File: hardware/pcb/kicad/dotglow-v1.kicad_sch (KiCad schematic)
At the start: 40 parts, among them J1 USB-C 5V, J2 DISPLAY IN, J3 DHT22, J4 I2C (RTC V2), J5 SPEAKER 8R 2W, J6 LDR, SW1 RESET, SW2 BOOT, SW3 STOPWATCH, U1 ESP32-S3-MINI-1-N8, U2 AP2112K-3.3, U3 74AHCT125, U4 MAX98357A, U5 USBLC6-2SC6

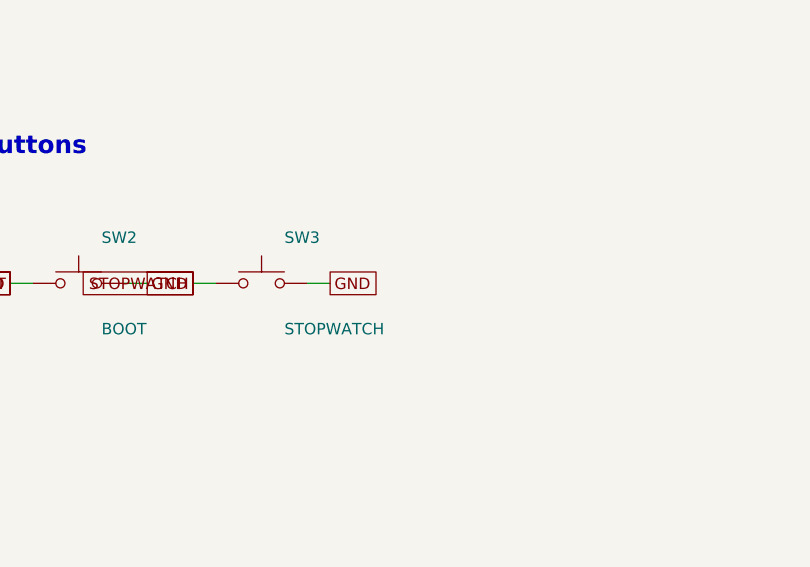
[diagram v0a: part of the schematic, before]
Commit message: DotGlow V1 board: stopwatch header J7, routing rerun, layout-only package for EasyEDA (outline, DXF, placement CSV)
Co-Authored-By: ElectroIoT <electroiot.in@gmail.com>
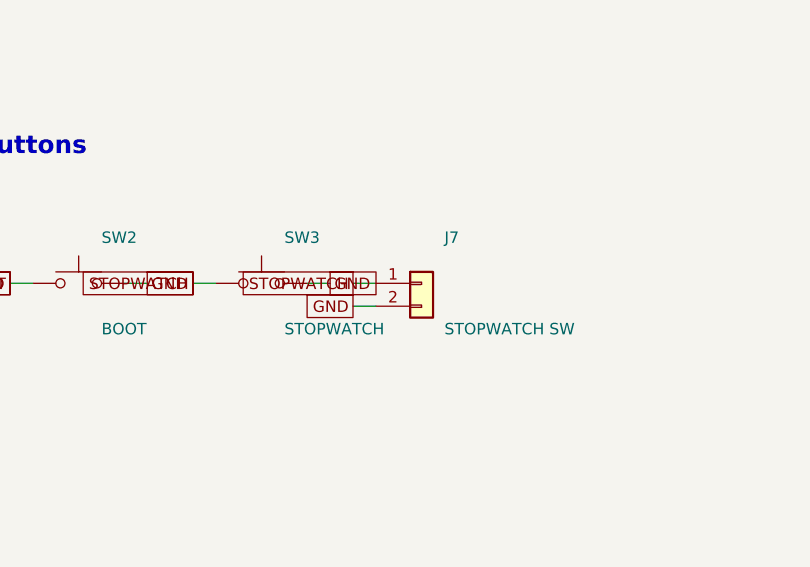
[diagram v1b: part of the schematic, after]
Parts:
- added J7: STOPWATCH SW, Connector_PinHeader_2.54mm:PinHeader_1x02_P2.54mm_Vertical, symbol Connector_Generic:Conn_01x02
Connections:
- net GND: now also J7.2 (Pin_2)
- net STOPWATCH: now also J7.1 (Pin_1)
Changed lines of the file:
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@@
+	)
+	(symbol
+		(lib_id "Connector_Generic:Conn_01x02")
+		(at 243.84 93.98 0)
+		(unit 1)
+		(exclude_from_sim no)
+		(in_bom yes)
+		(on_board yes)
+		(dnp no)
+		(property "Reference" "J7"
+			(at 246.38 88.9 0)
+			(effects
+				(font
+					(size 1.27 1.27)
+				)
+				(justify left)
+			)
+		)
+		(property "Value" "STOPWATCH SW"
+			(at 246.38 99.06 0)
+			(effects
+				(font
+					(size 1.27 1.27)
+				)
+				(justify left)
+			)
+		)
+		(property "Footprint" "Connector_PinHeader_2.54mm:PinHeader_1x02_P2.54mm_Vertical"
+			(at 243.84 93.98 0)
+			(hide yes)
+			(effects
+				(font
+					(size 1.27 1.27)
+				)
+			)
+		)
+		(property "Datasheet" ""
+			(at 243.84 93.98 0)
+			(hide yes)
+			(effects
+				(font
+					(size 1.27 1.27)
+				)
+			)
+		)
+		(pin "1"
+		)
+		(pin "2"
+		)
+		(instances
+			(project "dotglow-v1"
+				(path "/6d0007f9-f727-53d9-924c-8f566d92db0b"
+					(reference "J7")
+					(unit 1)
+				)
+			)
+		)
+	)
+	(wire
+		(pts
+			(xy 238.76 93.98)
+			(xy 236.22 93.98)
+		)
+		(stroke
+			(width 0)
+			(type default)
+		)
+	)
+	(global_label "STOPWATCH"
+		(shape passive)
+		(at 236.22 93.98 180)
+		(fields_autoplaced yes)
+		(effects
+			(font
+				(size 1.27 1.27)
+			)
+			(justify right)
+		)
+		(property "Intersheetrefs" "${INTERSHEET_REFS}"
+			(at 236.22 93.98 0)
+			(hide yes)
+			(effects
+				(font
+					(size 1.27 1.27)
+				)
+			)
+		)
+	)
+	(wire
+		(pts
+			(xy 238.76 96.52)
+			(xy 236.22 96.52)
+		)
+		(stroke
+			(width 0)
+			(type default)
+		)
+	)
+	(global_label "GND"
+		(shape passive)
+		(at 236.22 96.52 180)
+		(fields_autoplaced yes)
+		(effects
+			(font
+				(size 1.27 1.27)
+			)
+			(justify right)
+		)
+		(property "Intersheetrefs" "${INTERSHEET_REFS}"
+			(at 236.22 96.52 0)
+			(hide yes)
+			(effects
+				(font
+					(size 1.27 1.27)
+				)
+			)
+		)
 	)
 	(symbol

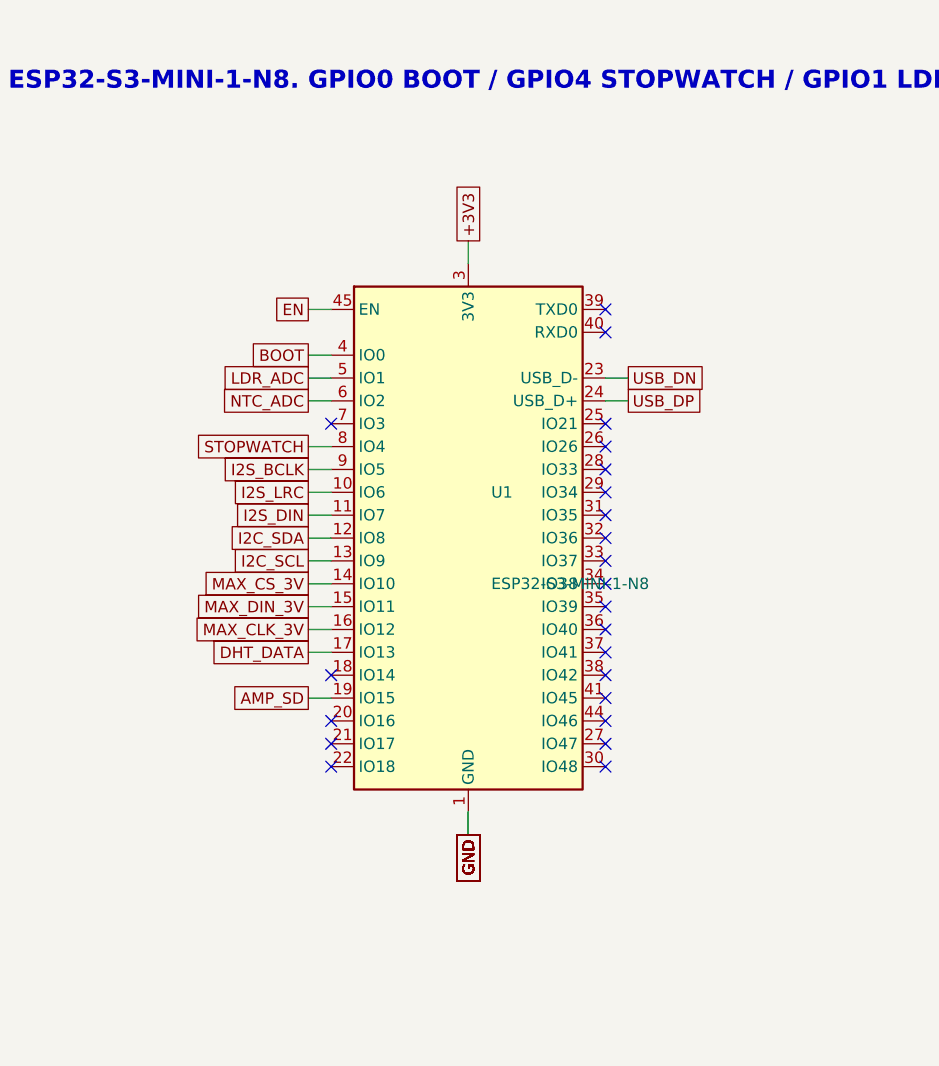
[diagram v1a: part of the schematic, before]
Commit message: DotGlow V1 board: switch to ESP32-S3-WROOM-1-N16R8 (C2913202), full pinout doc, display header on the module end, rebuild script
Co-Authored-By: ElectroIoT <electroiot.in@gmail.com>
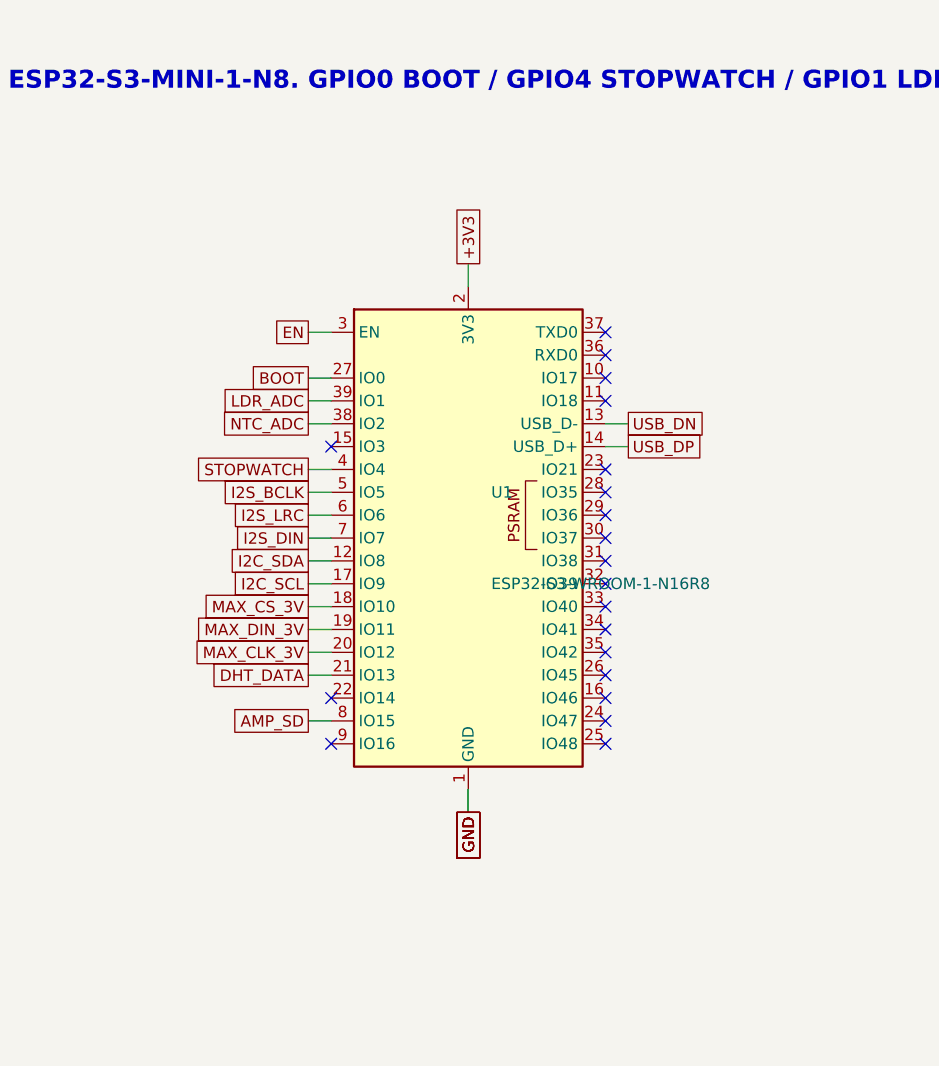
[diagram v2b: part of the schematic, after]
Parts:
- U1: value ESP32-S3-MINI-1-N8 -> ESP32-S3-WROOM-1-N16R8; footprint RF_Module:ESP32-S2-MINI-1 -> RF_Module:ESP32-S3-WROOM-1; symbol RF_Module:ESP32-S3-MINI-1 -> RF_Module:ESP32-S3-WROOM-1
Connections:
- net +3V3: now also U1.2 (3V3); no longer U1.3 (3V3)
- net AMP_SD: now also U1.8 (IO15); no longer U1.19 (IO15)
- net BOOT: now also U1.27 (IO0); no longer U1.4 (IO0)
- net DHT_DATA: now also U1.21 (IO13); no longer U1.17 (IO13)
- net EN: now also U1.3 (EN); no longer U1.45 (EN)
- net GND: now also U1.40 (GND), U1.41 (GND); no longer U1.2 (GND), U1.42 (GND), U1.43 (GND), U1.46 (GND), U1.47 (GND), U1.48 (GND), U1.49 (GND), U1.50 (GND), U1.51 (GND), U1.52 (GND), U1.53 (GND), U1.54 (GND), U1.55 (GND), U1.56 (GND), U1.57 (GND), U1.58 (GND), U1.59 (GND), U1.60 (GND), U1.61 (GND), U1.62 (GND), U1.63 (GND), U1.64 (GND), U1.65 (GND)
- net I2C_SCL: now also U1.17 (IO9); no longer U1.13 (IO9)
- net I2S_BCLK: now also U1.5 (IO5); no longer U1.9 (IO5)
- net I2S_DIN: now also U1.7 (IO7); no longer U1.11 (IO7)
- net I2S_LRC: now also U1.6 (IO6); no longer U1.10 (IO6)
- net LDR_ADC: now also U1.39 (IO1); no longer U1.5 (IO1)
- net MAX_CLK_3V: now also U1.20 (IO12); no longer U1.16 (IO12)
- net MAX_CS_3V: now also U1.18 (IO10); no longer U1.14 (IO10)
- net MAX_DIN_3V: now also U1.19 (IO11); no longer U1.15 (IO11)
- net NTC_ADC: now also U1.38 (IO2); no longer U1.6 (IO2)
- net STOPWATCH: now also U1.4 (IO4); no longer U1.8 (IO4)
- net USB_DN: now also U1.13 (USB_D-); no longer U1.23 (USB_D-)
- net USB_DP: now also U1.14 (USB_D+); no longer U1.24 (USB_D+)
- no-connect marks 27 -> 24

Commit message: DotGlow V1 board: JST XA connectors (2-pin C265077, 3-pin C265055, 4-pin C491709) for speaker, stopwatch, LDR, DHT22, I2C; re-placed and re-routed
Co-Authored-By: ElectroIoT <electroiot.in@gmail.com>
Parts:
- J3: footprint Connector_PinHeader_2.54mm:PinHeader_1x03_P2.54mm_Vertical -> Connector_JST:JST_XA_B03B-XASK-1_1x03_P2.50mm_Vertical
- J4: footprint Connector_PinHeader_2.54mm:PinHeader_1x04_P2.54mm_Vertical -> Connector_JST:JST_XA_B04B-XASK-1-A_1x04_P2.50mm_Vertical
- J5: footprint Connector_JST:JST_PH_S2B-PH-K_1x02_P2.00mm_Horizontal -> Connector_JST:JST_XA_B02B-XASK-1-A_1x02_P2.50mm_Vertical
- J6, J7: footprint Connector_PinHeader_2.54mm:PinHeader_1x02_P2.54mm_Vertical -> Connector_JST:JST_XA_B02B-XASK-1-A_1x02_P2.50mm_Vertical
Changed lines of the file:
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@@
 			)
 		)
-		(property "Footprint" "Connector_PinHeader_2.54mm:PinHeader_1x02_P2.54mm_Vertical"
+		(property "Footprint" "Connector_JST:JST_XA_B02B-XASK-1-A_1x02_P2.50mm_Vertical"
 			(at 243.84 93.98 0)
 			(hide yes)
@@
 			)
 		)
-		(property "Footprint" "Connector_JST:JST_PH_S2B-PH-K_1x02_P2.00mm_Horizontal"
+		(property "Footprint" "Connector_JST:JST_XA_B02B-XASK-1-A_1x02_P2.50mm_Vertical"
 			(at 248.92 215.9 0)
 			(hide yes)
@@
 			)
 		)
-		(property "Footprint" "Connector_PinHeader_2.54mm:PinHeader_1x02_P2.54mm_Vertical"
+		(property "Footprint" "Connector_JST:JST_XA_B02B-XASK-1-A_1x02_P2.50mm_Vertical"
 			(at 205.74 264.16 0)
 			(hide yes)
@@
 			)
 		)
-		(property "Footprint" "Connector_PinHeader_2.54mm:PinHeader_1x03_P2.54mm_Vertical"
+		(property "Footprint" "Connector_JST:JST_XA_B03B-XASK-1_1x03_P2.50mm_Vertical"
 			(at 243.84 264.16 0)
 			(hide yes)
@@
 			)
 		)
-		(property "Footprint" "Connector_PinHeader_2.54mm:PinHeader_1x04_P2.54mm_Vertical"
+		(property "Footprint" "Connector_JST:JST_XA_B04B-XASK-1-A_1x04_P2.50mm_Vertical"
 			(at 284.48 264.16 0)
 			(hide yes)

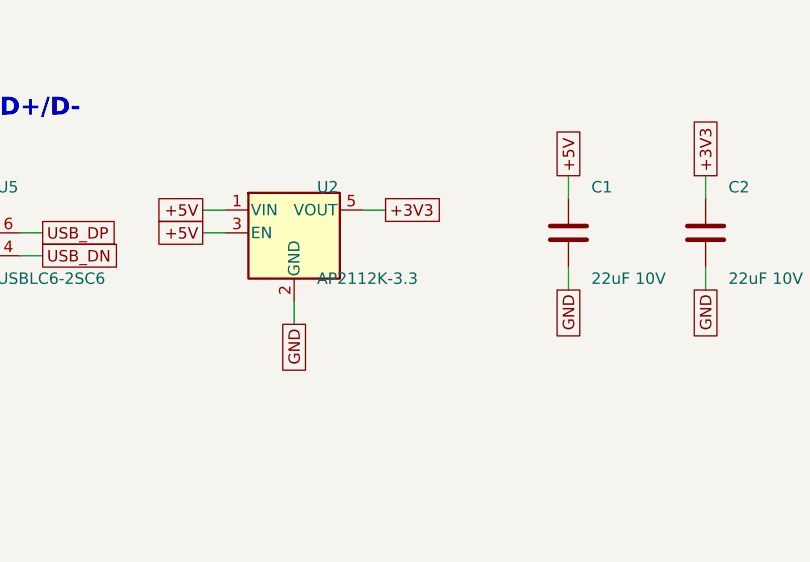
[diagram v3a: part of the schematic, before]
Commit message: DotGlow V1 board: final EasyEDA files (schematic, PCB, BOM, Gerber), 3D renders and viewer angles, README banner, HyperFrames short video source
Co-Authored-By: ElectroIoT <electroiot.in@gmail.com>
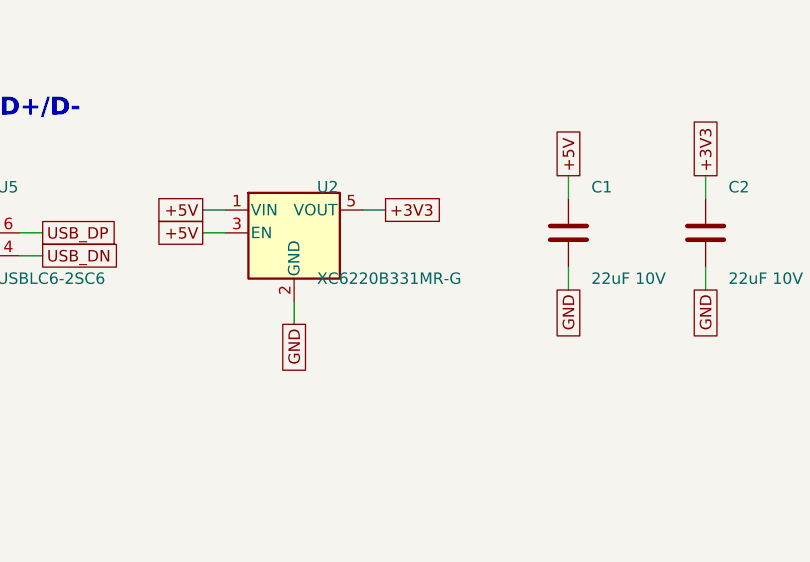
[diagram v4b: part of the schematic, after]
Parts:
- U2: value AP2112K-3.3 -> XC6220B331MR-G
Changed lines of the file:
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@@
 			)
 		)
-		(property "Value" "AP2112K-3.3"
+		(property "Value" "XC6220B331MR-G"
 			(at 302.26 45.72 0)
 			(effects
